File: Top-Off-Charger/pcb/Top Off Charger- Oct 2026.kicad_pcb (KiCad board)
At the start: 2 copper layers, 31.5 x 95 mm, 18 parts, among them U1 Xiao ESP32C3, U2 Adafruit INA228 5832, U3 Pololu D24V7F3, U4 Big MOSFET Slide Switch with 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, U5 Pololu Ideal Diode Reverse Vo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

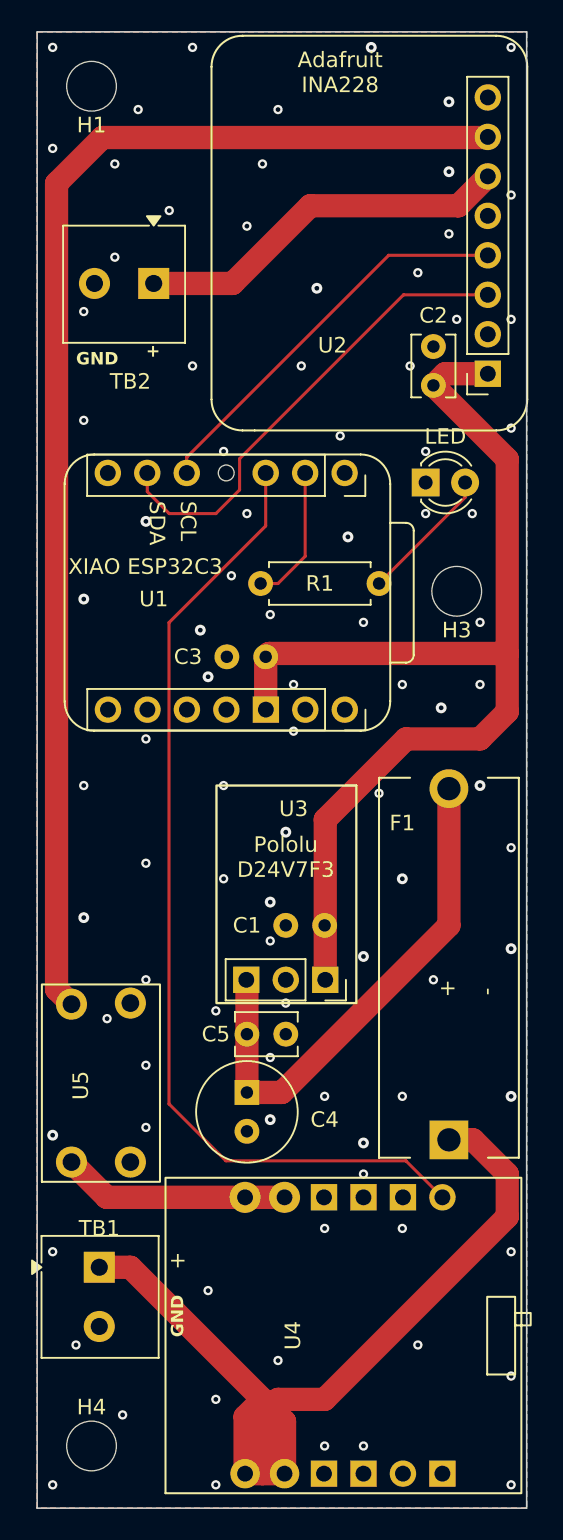
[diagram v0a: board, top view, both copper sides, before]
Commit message: Top-Off Charger: rev 0.7 board, re-laid 29.5 x 78 mm, and design rev 0.7
- Top-Off-Charger/pcb/: the owner's re-laid board replaces v7 (saved
  2026-10-06 15:16:19, 309,671 B, sha256 be94508f8888b7a4...). Its
  .kicad_pro differs from v7's only in the default width of new pads
  and the last plot path, so the design rules are unchanged. KiCad 10
  DRC (--severity-all --refill-zones): 0 errors, 26 warnings (all silk
  or library), 0 unconnected. Schematic parity did not run (no
  schematic). Gerbers not exported (O11).
- gnd_drop.py: it took pad 2 of each terminal block as GND; rev 0.7
  moved TB1's GND to pad 1 and it stopped with "expected two
  terminal-block GND pads". It now finds TB2's and TB1's GND pads by
  reference and net (R13 note at the site). --self-test gains a third
  direction, a board with no TB2 is refused: SELF-TEST PASSED.
- Design doc rev 0.7: TB1's pins swapped (PSU +V on the lower screw);
  TB1/TB2 named as Phoenix 5442756 (O9 closed); LED moved and turned
  180 degrees; XIAO D6/D7 unplated; GPIO4_SW, SDA and SCL on B.Cu;
  assembly order for the parts under the modules. 7.3 compares the
  electrical figures with rev 0.6, including what the B.Cu tracks cost
  the ground pour.
- CHANGELOG: 2026-10-06 Changed and Fixed entries.

Co-Authored-By: Claude Opus 5.5 <noreply@anthropic.com>
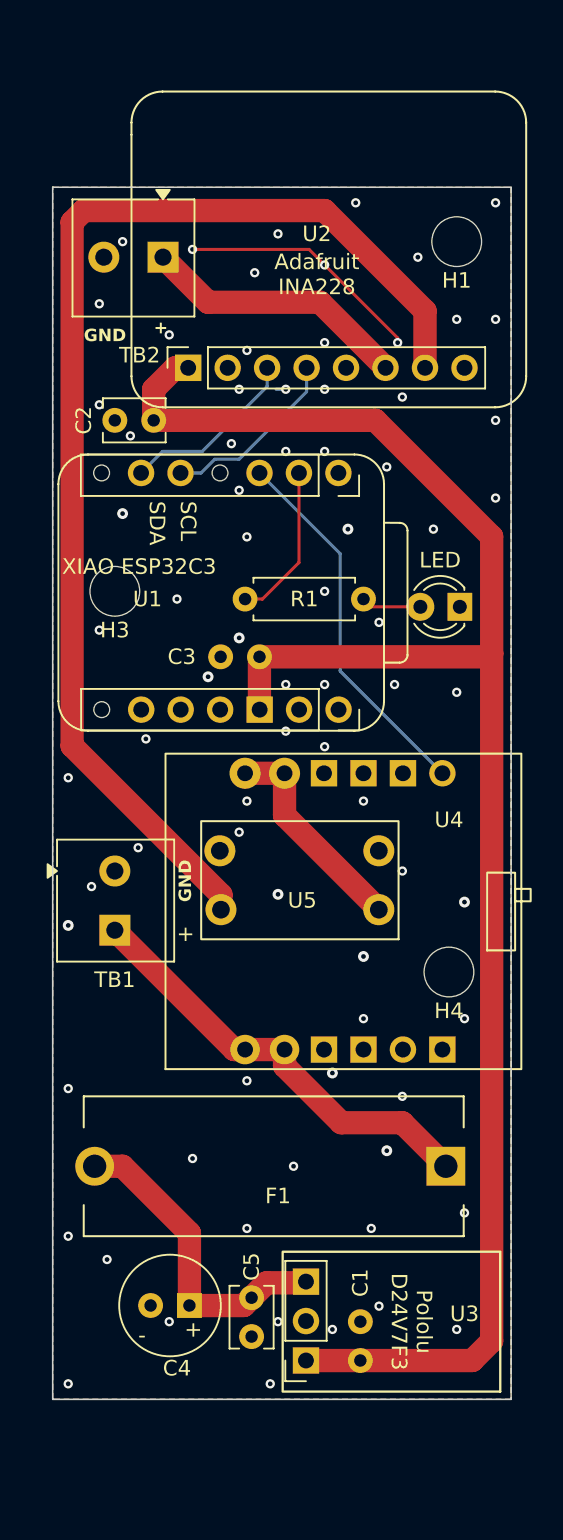
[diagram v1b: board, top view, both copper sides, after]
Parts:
- C1: value CAP CER 10UF 10% 25V X7R RADIAL -> CAP CER 10UF 10% 25V X7R RADIAL, FG18X5R1E106MRT00
- C2, C3, C5: value CAP CER 0.1UF 50V X7R RADIAL -> CAP CER 0.1UF 50V X7R RADIAL, K104K10X7RF53L2
- C4: value 47uF 50V Radial Capacitor -> CAP ALUM 47UF 20% 50V RADIAL TH, EEU-FR1H470
- F1: value 1A SB Wurth 696108003002 -> FUSEHOLDER BLOCKS - PCB - CLIP C, 696108003002
- R1: value 1 kOhms ±5% 0.25W, 1/4W Through Hole Resistor Axial Carbon Film -> 1 kOhms ±5% 0.25W, 1/4W Through Hole Resistor Axial Carbon Film, CF14JT1K00
- TB1, TB2: value TerminalBlock_Phoenix_MKDS-1-2-3.81_1x02_P3.81mm_Horizontal -> TERM BLK 2P SIDE ENT 3.81MM PCB, 5442756
- moved H4 38.2 mm to (39.0, 70.5)
- moved C1 28.1 mm to (33.3, 95.5), turned to 90 degrees
- moved U5 27.8 mm to (35.8, 60.8), turned to 180 degrees
- moved U4 27.3 mm to (43.7, 76.8)
- moved H1 25.5 mm to (39.5, 23.5)
- moved TB1 25.5 mm to (17.5, 64.0)
- moved U3 24.5 mm to (29.8, 95.5), turned to 180 degrees
- moved H3 22.0 mm to (17.5, 46.0)
- moved C2 21.0 mm to (17.5, 35.0), turned to 0 degrees
- moved U2 20.3 mm to (22.2, 32.6), turned to 90 degrees
- moved C5 19.6 mm to (26.3, 94.0), turned to 90 degrees
- moved F1 17.4 mm to (27.5, 83.0), turned to 180 degrees
- moved C4 14.2 mm to (22.3, 92.0), turned to 180 degrees
- moved LED 8.30 mm to (39.7, 47.0), turned to 180 degrees
- moved TB2 1.79 mm to (20.6, 24.5)
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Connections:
- TB1 pad 1: BATT_RAW -> GND
- TB1 pad 2: GND -> BATT_RAW
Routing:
- net +3V3: track 70.7 -> 112.3 mm
- net GPIO4_SW: track 63.3 -> 24.2 mm
- net BATT_RAW: track 59.7 -> 28.2 mm
- net SCL: track 30.7 -> 11.6 mm
- net GND: track 0.00 -> 16.5 mm, vias 92 -> 77
- net SDA: track 25.8 -> 11.8 mm
- net V_Fused: track 33.5 -> 20.6 mm
- net VIN-: track 24.4 -> 17.3 mm
- net GPIO3_LED: track 8.79 -> 3.87 mm
- net VIN+: track 82.1 -> 77.6 mm
- net GPIO3: track 8.96 -> 10.2 mm
- net Batt_SW: track 14.7 -> 13.8 mm
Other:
- board size 31.5 x 95 mm -> 29.5 x 78 mm
- board text added: "Board Size: 29.5mm x 78mm 1 3/16{dblquote} x 3 1/16{dblquote}"
- board text removed: "Board Size: 31.5mm x 90mm 1 1/4{dblquote} x 3 1/2{dblquote}"

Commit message: Top-Off Charger: Kelvin GND for the INA228, and design section 7.4
- Top-Off-Charger/pcb/: the owner's 17:09:17 save of the same board
  (309,654 B, sha256 484347efc18dab89...) adds a Kelvin GND. U2 pin 2
  moves to a new net, GND_SENSE, joined to GND at TB2-2's pad by a net
  tie (reference still REF**, rename to NT1 is O16) and a 0.5 mm F.Cu
  track. The .kicad_pro differs only in the default size and drill of
  new pads. DRC: 0 errors, 26 warnings, 0 unconnected, the same 26
  entries as the 15:16 save. A GND track injected onto the GND_SENSE
  track fires clearance and shorting_items.
- Design doc, still rev 0.7: the Kelvin GND takes the VBUS offset from
  1.37-1.39 mV to <= 0.20 mV at 3.64 A [D] (5, 7.3). Lead is 24-30 in
  (owner), so 6.4's example drops 58-73 mV at 3.64 A [D], not 146 (5 ft).
  The 7.3/T10 falsifier now probes the solder joints, not TB2-2's screw
  (R13 note at the site). New 7.4: the improvement study, and the
  baseline and 9-step method for evaluating the owner's planned B.Cu
  VIN+ re-route (O15, before the Gerbers). O11 updated, O16 added.
- CHANGELOG: two 2026-10-06 Changed entries and one Fixed.

Co-Authored-By: Claude Opus 5.5 <noreply@anthropic.com>
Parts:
- added REF**: NetTie-2_SMD_Pad0.5mm, NetTie:NetTie-2_SMD_Pad0.5mm, F.Cu at (17.9, 25.5)
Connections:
- U2 pad 2: GND -> GND_SENSE
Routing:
- net GND_SENSE: track 0.00 -> 8.87 mm
- net GND: vias 77 -> 78
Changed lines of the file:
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@@
 		)
 	)
+	(footprint "NetTie:NetTie-2_SMD_Pad0.5mm"
+		(layer "F.Cu")
+		(at 17.91 25.5 -41.8)
+		(descr "Net tie, 2 pin, 0.5mm square SMD pads")
+		(tags "net tie")
+		(property "Reference" "REF**"
+			(at 0 -1.2 138.2)
+			(layer "F.SilkS")
+			(hide yes)
+			(effects
+				(font
+					(size 1 1)
+					(thickness 0.15)
+				)
+			)
+		)
+		(property "Value" "NetTie-2_SMD_Pad0.5mm"
+			(at 0 1.2 138.2)
+			(layer "F.Fab")
+			(hide yes)
+			(effects
+				(font
+					(size 1 1)
+					(thickness 0.15)
+				)
+			)
+		)
+		(property "Datasheet" ""
+			(at 0 0 318.2)
+			(unlocked yes)
+			(layer "F.Fab")
+			(hide yes)
+			(effects
+				(font
+					(size 1.27 1.27)
+					(thickness 0.15)
+				)
+			)
+		)
+		(property "Description" ""
+			(at 0 0 318.2)
+			(unlocked yes)
+			(layer "F.Fab")
+			(hide yes)
+			(effects
+				(font
+					(size 1.27 1.27)
+					(thickness 0.15)
+				)
+			)
+		)
+		(attr exclude_from_pos_files exclude_from_bom allow_missing_courtyard)
+		(net_tie_pad_groups "1, 2")
+		(duplicate_pad_numbers_are_jumpers no)
+		(fp_poly
+			(pts
+				(xy -0.5 -0.25) (xy 0.5 -0.25) (xy 0.5 0.25) (xy -0.5 0.25)
+			)
+			(stroke
+				(width 0)
+				(type solid)
+			)
+			(fill yes)
+			(layer "F.Cu")
+		)
+		(pad "1" smd circle
+			(at -0.5 0 318.2)
+			(size 0.5 0.5)
+			(layers "F.Cu")
+			(net "GND")
+		)
+		(pad "2" smd circle
+			(at 0.5 0 318.2)
+			(size 0.5 0.5)
+			(layers "F.Cu")
+			(net "GND_SENSE")
+		)
+		(embedded_fonts no)
+	)
 	(footprint "Adafruit INA260:Adafruit INA228"
 		(layer "F.Cu")
@@
 			(layers "*.Cu" "*.Mask")
 			(remove_unused_layers no)
-			(net "GND")
+			(net "GND_SENSE")
 		)
 		(pad "3" thru_hole oval
@@
 			(remove_unused_layers no)
 			(net "GND")
+			(zone_connect 2)
 		)
 		(embedded_fonts no)
@@
 		(tags "THT Terminal Block Phoenix MKDS-1-2-3.81 pitch 3.81mm size 7.61x7.3mm drill 1.1mm pad 2mm")
 		(property "Reference" "TB1"
-			(at 7 0 0)
+			(at 9.5 0 0)
 			(layer "F.SilkS")
 			(effects
@@
 		)
 	)
-	(gr_text "+"
-		(at 20 29.5 0)
+	(gr_text "GND"
+		(at 16 61.5 0)
 		(layer "F.SilkS")
 		(effects
@@
 		)
 	)
-	(gr_text "GND"
-		(at 22.5 66 90)
+	(gr_text "+"
+		(at 20 29.5 0)
 		(layer "F.SilkS")
 		(effects
@@
 	)
 	(gr_text "+"
-		(at 21.5 67.5 270)
+		(at 17 70 270)
 		(layer "F.SilkS")
 		(effects
@@
 	)
 	(via
+		(at 23.5 29)
+		(size 0.6)
+		(drill 0.3)
+		(layers "F.Cu" "B.Cu")
+		(free yes)
+		(net "GND")
+	)
+	(via
 		(at 22.5 24)
 		(size 0.6)
@@
 	)
 	(via
-		(at 21 29.5)
+		(at 20.5 30)
 		(size 0.6)
 		(drill 0.3)
@@
 		(net "VIN+")
 	)
+	(segment
+		(start 23.14 30)
+		(end 24.76 31.62)
+		(width 0.5)
+		(layer "F.Cu")
+		(net "GND_SENSE")
+	)
+	(segment
+		(start 22.449472 30)
+		(end 23.14 30)
+		(width 0.5)
+		(layer "F.Cu")
+		(net "GND_SENSE")
+	)
+	(segment
+		(start 18.282738 25.833266)
+		(end 22.449472 30)
+		(width 0.5)
+		(layer "F.Cu")
+		(net "GND_SENSE")
+	)
 	(zone

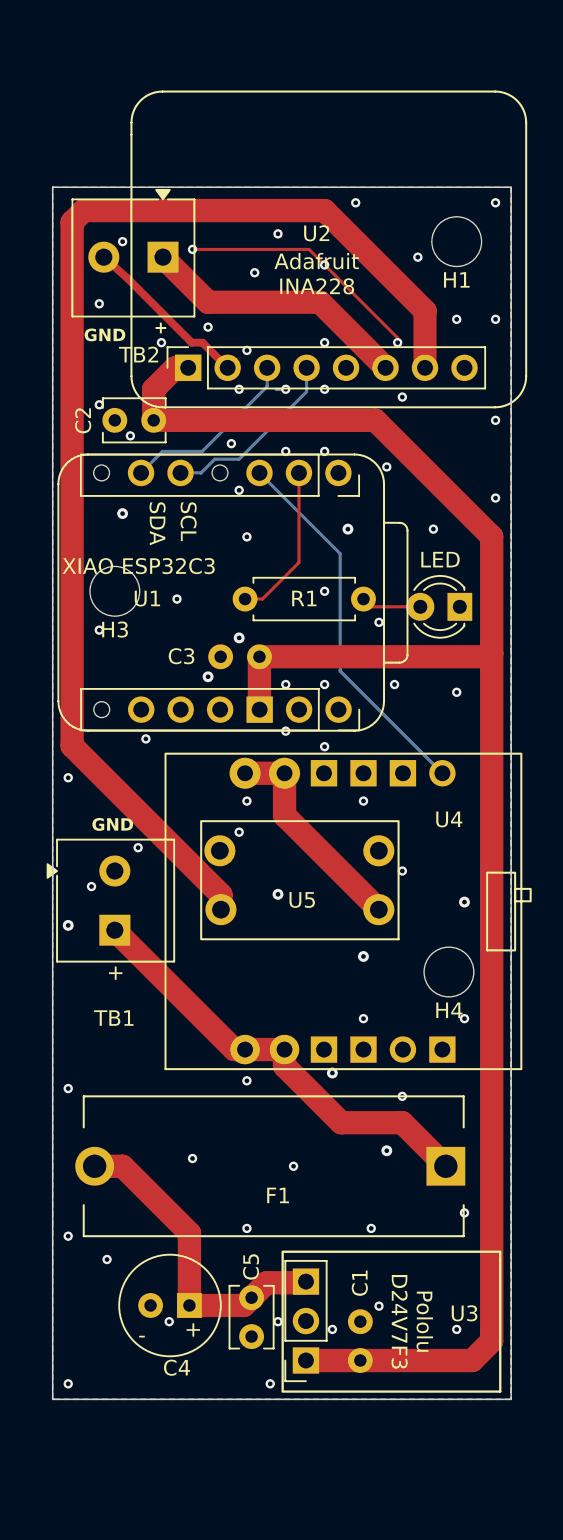
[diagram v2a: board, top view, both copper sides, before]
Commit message: Top-Off Charger: rev 0.8 board (VIN+ on B.Cu, wider power path)
Board files in pcb/ are the owner's 2026-10-08 11:00:58 save
(sha256 e5586ceb...efaf). All checks ran on the 10:48:22 save
(9661db54...5b28); the 11:00 save adds only U1 3D models, and its
DRC set is identical.

Gate: DRC 0 errors / 34 warnings / 0 unconnected (+11/-3 vs rev 0.7,
each named in section 7). Schematic parity DID NOT RUN (no schematic).
No pad's net changed.

Design doc rev 0.8:
- 6.4: new widths and IPC figures; charge-path track 37.33 -> 12.17
  mOhm [D, 2-D solve]; F1 branch width is board supply only.
- 5.1 / 5.5: TB1 moved 4.5 mm down, so its labels can be read with
  U4 seated. The LED is now on the left edge, so the anode (round)
  hole is the one nearer the board edge. Polarity table rewritten.
- 7 / 7.3 / 7.4: rev 0.8 identity, gate verdicts, pour and Kelvin
  figures, the VIN+ re-route outcome, and an R13 record of the edits
  a review session wrote into the board on 2026-10-06.
- 12: O12 and O15 closed; O11, O13, O14 and O16 revised.
  Gerbers still to export (O11).

Co-Authored-By: Claude Opus 5.5 <noreply@anthropic.com>
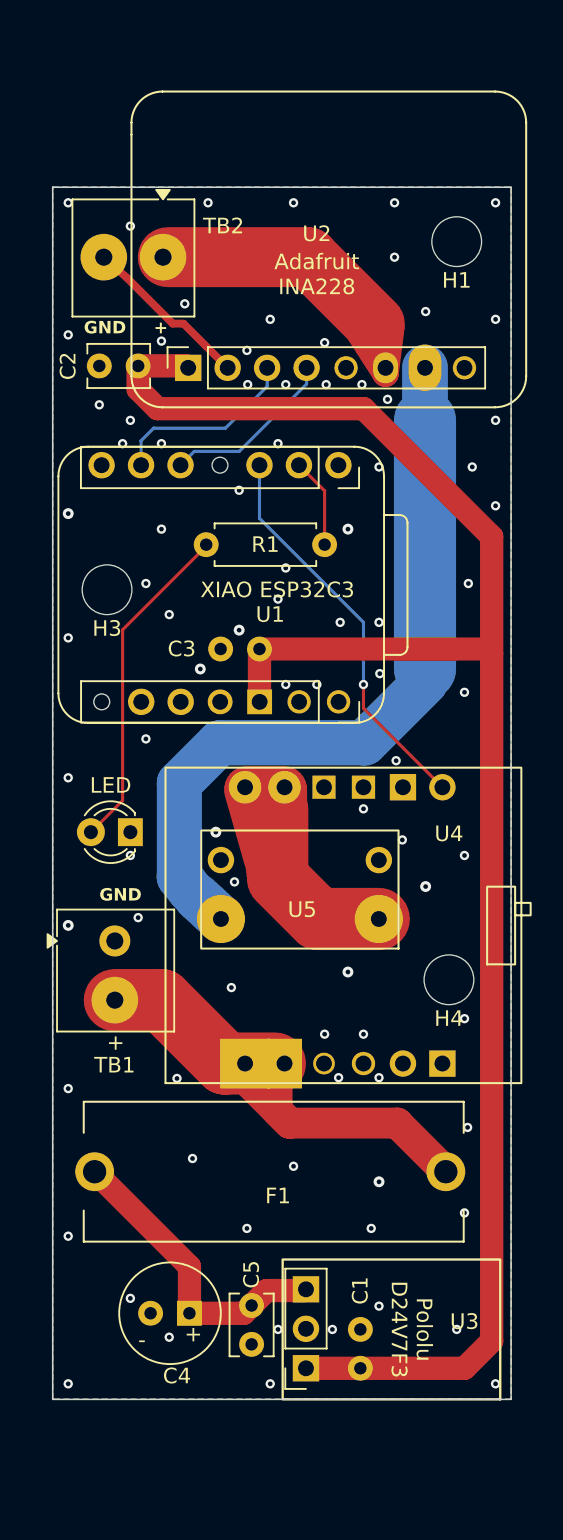
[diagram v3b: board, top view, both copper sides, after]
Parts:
- moved LED 25.7 mm to (18.5, 61.5)
- moved R1 6.20 mm to (31.0, 43.0), turned to 180 degrees
- moved TB1 4.50 mm to (17.5, 68.5)
- moved C2 3.64 mm to (16.5, 31.5)
- moved U4 0.90 mm to (43.7, 77.7)
- moved U5 0.60 mm to (35.8, 61.4)
- moved H3 0.51 mm to (17.0, 45.9)
- moved C1 0.50 mm to (33.3, 96.0)
- moved C3 0.50 mm to (24.3, 49.7)
- moved C4 0.50 mm to (22.3, 92.5)
- moved C5 0.50 mm to (26.3, 94.5)
- moved H4 0.50 mm to (39.0, 71.0)
- moved U1 0.50 mm to (16.7, 37.9)
- moved U3 0.50 mm to (29.8, 96.0)
- moved F1 0.35 mm to (27.5, 83.3)
- renumbered REF** to NT1
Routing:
- net VIN+: track 77.6 -> 47.3 mm
- net GPIO3_LED: track 3.87 -> 21.5 mm
- net GND: track 16.5 -> 0.00 mm, vias 78 -> 85
- net Batt_SW: track 13.8 -> 21.6 mm
- net VIN-: track 17.3 -> 21.9 mm
- net BATT_RAW: track 28.2 -> 32.5 mm
- net GPIO3: track 10.2 -> 6.30 mm
- net +3V3: track 112.3 -> 114.3 mm
- net GPIO4_SW: track 24.2 -> 25.6 mm, vias 0 -> 1
- net V_Fused: track 20.6 -> 19.7 mm
- net SCL: track 11.6 -> 12.3 mm
- net SDA: track 11.8 -> 11.3 mm
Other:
- board text removed: "SCL"
- board text removed: "SDA"
